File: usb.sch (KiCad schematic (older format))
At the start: 2 parts

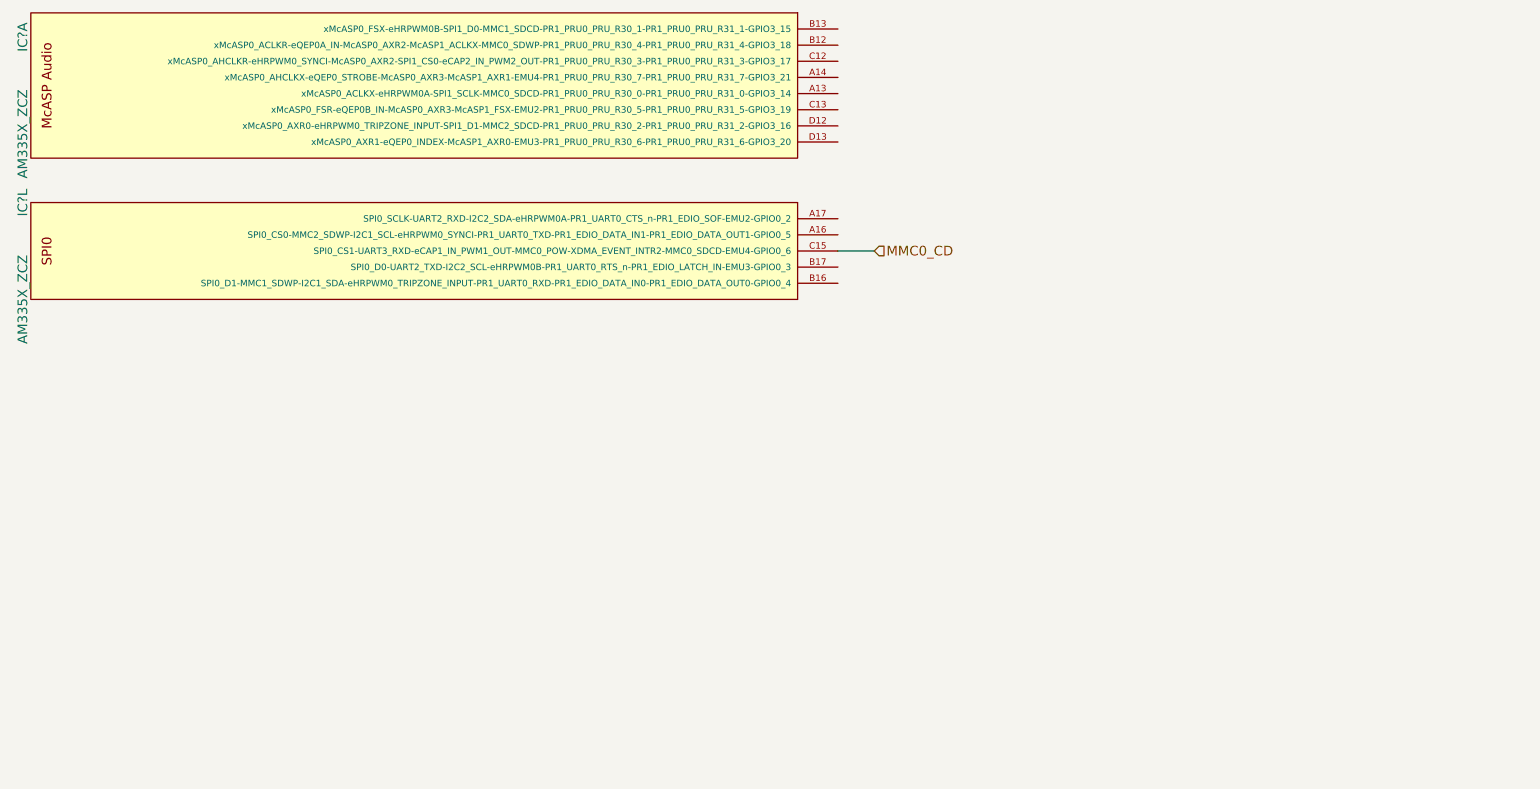
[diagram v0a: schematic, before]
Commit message: emmc nand and micro sd
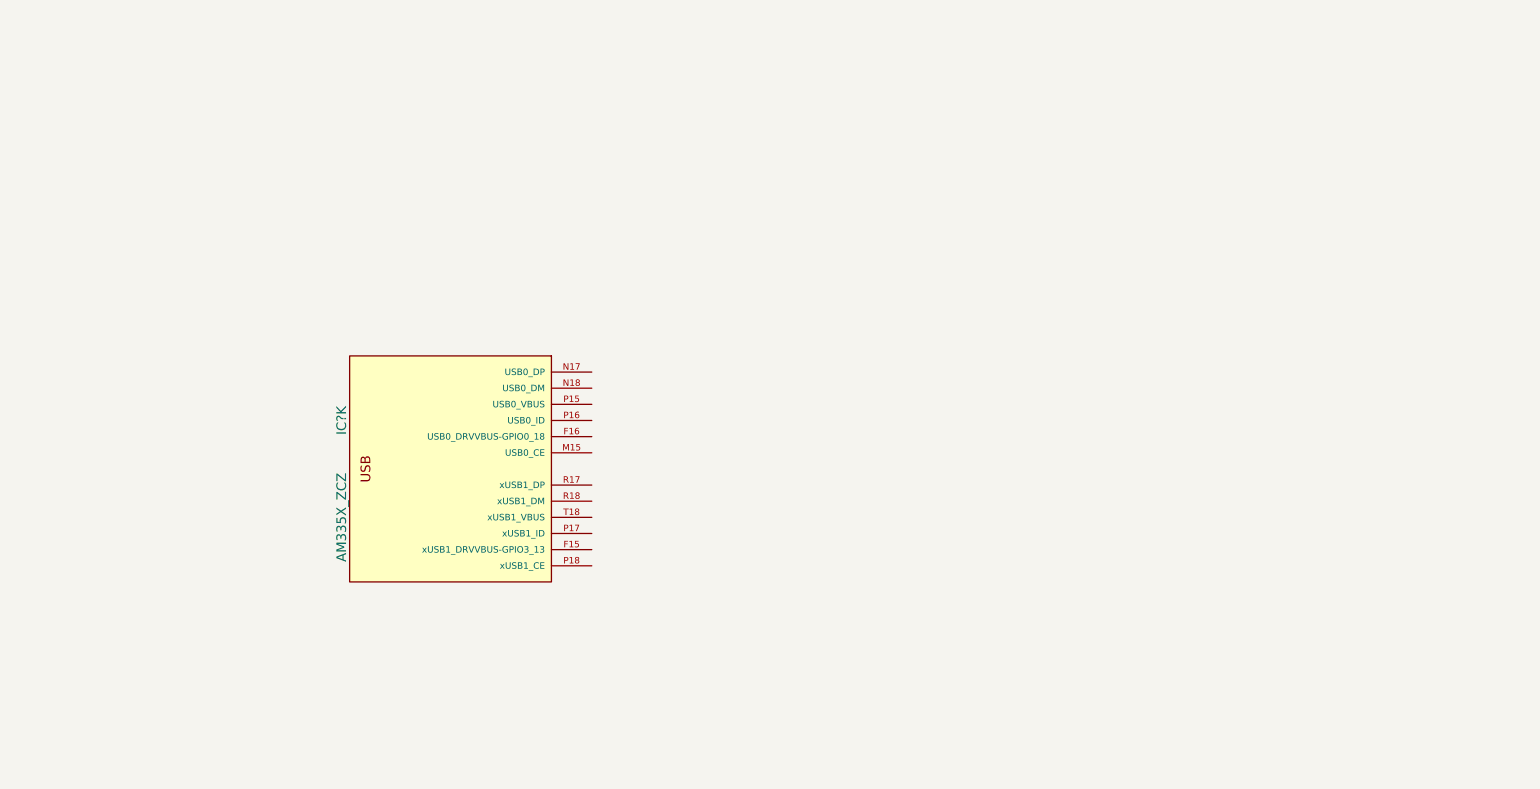
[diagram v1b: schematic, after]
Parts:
- removed IC? (x2): AM335X_ZCZ, symbol AM335X_ZCZ
- added IC?: AM335X_ZCZ, symbol AM335X_ZCZ
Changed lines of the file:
@@
 $Descr A4 11693 8268
 encoding utf-8
-Sheet 4 8
+Sheet 8 8
 Title ""
 Date ""
@@
 $Comp
 L AM335X_ZCZ IC?
-U 1 1 589C81F5
-P 675 1050
-F 0 "IC?" V 625 1350 60  0000 C CNN
-F 1 "AM335X_ZCZ" V 625 750 60  0000 C CNN
-F 2 "" H 675 1050 60  0001 C CNN
-F 3 "" H 675 1050 60  0001 C CNN
-	1    675  1050
+U 11 1 58AF2AA9
+P 2650 3425
+F 0 "IC?" V 2600 3725 60  0000 C CNN
+F 1 "AM335X_ZCZ" V 2600 3125 60  0000 C CNN
+F 2 "" H 2650 3425 60  0001 C CNN
+F 3 "" H 2650 3425 60  0001 C CNN
+	11   2650 3425
 	1    0    0    -1
 $EndComp
-$Comp
-L AM335X_ZCZ IC?
-U 12 1 58AE72E9
-P 675 2075
-AR Path="/58AE72E9" Ref="IC?"  Part="12"
-AR Path="/589C7F89/58AE72E9" Ref="IC?"  Part="12"
-F 0 "IC?" V 625 2375 60  0000 C CNN
-F 1 "AM335X_ZCZ" V 625 1775 60  0000 C CNN
-F 2 "" H 675 2075 60  0001 C CNN
-F 3 "" H 675 2075 60  0001 C CNN
-	12   675  2075
-	1    0    0    -1
-$EndComp
-Wire Wire Line
-	5675 2075 5900 2075
-Text HLabel 5900 2075 2    60   Input ~ 0
-MMC0_CD
 $EndSCHEMATC

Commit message: usb
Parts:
- added C? (x2): 100nF/6.3V, symbol C
- added C?: 100uF/6.3V, symbol CP
- added L?: 0.1ohm 0805, symbol L
- added L?: 150ohm 1000mA, symbol L
- added R? (x2): 0R, symbol R
- added R? (x2): 10k, symbol R
- added U? (x2): TPD4S012, symbol TPD4S012
- added U?: TPS2065CDGN, symbol TPS2065CDGN
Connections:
- net USB1_DRVVBUS: now reaches IC?.F15 (xUSB1_DRVVBUS-GPIO3_13)
- net USB1_DRVVBUS: now also R?.1, U?.4 (EN)
- net USB0_DP: now reaches IC?.N17 (USB0_DP)
- net USB0_DP: now also U?.1 (D+)
- net USB0_DM: now reaches IC?.N18 (USB0_DM)
- net USB0_DM: now also U?.2 (D-)
- net at IC?.P15 (USB0_VBUS): now also R?.2
- net USB0_ID: now reaches IC?.P16 (USB0_ID)
- net USB0_ID: now also U?.3 (ID)
- net at IC?.P17 (xUSB1_ID): now also R?.2
- net USB1_DP: now reaches IC?.R17 (xUSB1_DP)
- net USB1_DP: now also U?.1 (D+)
- net USB1_DM: now reaches IC?.R18 (xUSB1_DM)
- net USB1_DM: now also U?.2 (D-)
- net at IC?.T18 (xUSB1_VBUS): now also L?.2
- new net GNDD: C?.2, C?.2, C?.2, R?.1, R?.2, U?.1 (GND), U?.4 (GND), U?.4 (GND), U?.9 (PAD)
- new net SYS_5V: C?.1, U?.2 (IN), U?.3 (IN)
- new net USB1_OCn: R?.2, U?.5 (~FLT)
- new net USB1_PWR: C?.1, L?.1, L?.2, U?.6 (OUT), U?.6 (VBUS), U?.7 (OUT), U?.8 (OUT)
- new net USB1_VBUS: L?.1
- new net USB_DC: C?.1, R?.1, U?.6 (VBUS)
- new net VDD_3V3A: R?.1
- no-connect marks 0 -> 4
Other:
- moved on the sheet: IC?K

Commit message: system sheet
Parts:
- IC?: footprint (none) -> footprints:PBGA_N324
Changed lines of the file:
@@
 LIBS:tpd4s012
 LIBS:tps2065cdgn
+LIBS:74lvc1g07dck
 LIBS:mateboard-cache
 EELAYER 25 0
@@
 F 0 "IC?" V 2250 2950 60  0000 C CNN
 F 1 "AM335X_ZCZ" V 2250 2350 60  0000 C CNN
-F 2 "" H 2300 2650 60  0001 C CNN
+F 2 "footprints:PBGA_N324" H 2300 2650 60  0001 C CNN
 F 3 "" H 2300 2650 60  0001 C CNN
 	11   2300 2650

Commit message: wip wifi
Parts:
- C?: value 100uF/6.3V -> 220uF/6.3V; footprint (none) -> Capacitors_Tantalum_SMD:CP_Tantalum_Case-A_EIA-3216-18_Reflow
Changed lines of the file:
@@
 P 6850 4025
 F 0 "C?" H 6875 4125 50  0000 L CNN
-F 1 "100uF/6.3V" H 6875 3925 50  0000 L CNN
-F 2 "" H 6888 3875 50  0000 C CNN
+F 1 "220uF/6.3V" H 6875 3925 50  0000 L CNN
+F 2 "Capacitors_Tantalum_SMD:CP_Tantalum_Case-A_EIA-3216-18_Reflow" H 6888 3875 50  0001 C CNN
 F 3 "" H 6850 4025 50  0000 C CNN
 	1    6850 4025
